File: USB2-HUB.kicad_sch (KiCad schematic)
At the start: 31 parts, among them J11 USB_OTG, J13 690-008-221-904, U13 FSUSB42MUX, U4 TPD4EUSB30, U6 USB2514B-I/M2, U7 AP22653W6, Y1 24MHz

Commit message: added a lot more parts
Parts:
- C11, C14, C15, C3, C4, C7: value 100n -> 0.1uF; DK (none) -> 478-KGM05AR71C104KHCT-ND; PARTNO (none) -> KGM05AR71C104KH; Part Description 0.1uF 10% 16V Ceramic Capacitor X7R 0402 (1005 Metric) -> (none)
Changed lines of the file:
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@@
       (effects (font (size 1.27 1.27)) (justify left))
     )
-    (property "Value" "100n" (at 119.761 170.053 0)
+    (property "Value" "0.1uF" (at 119.761 170.053 0)
       (effects (font (size 1.27 1.27)) (justify left))
     )
@@
       (effects (font (size 1.27 1.27)) hide)
     )
-    (property "Part Description" "	0.1uF 10% 16V Ceramic Capacitor X7R 0402 (1005 Metric)" (at 116.84 168.91 0)
+    (property "Part Description" "" (at 116.84 168.91 0)
       (effects (font (size 1.27 1.27)) hide)
     )
@@
       (effects (font (size 1.27 1.27)) hide)
     )
+    (property "DK" "478-KGM05AR71C104KHCT-ND" (at 116.84 168.91 0)
+      (effects (font (size 1.27 1.27)) hide)
+    )
+    (property "PARTNO" "KGM05AR71C104KH" (at 116.84 168.91 0)
+      (effects (font (size 1.27 1.27)) hide)
+    )
     (pin "1")
     (pin "2")
@@
       (effects (font (size 1.27 1.27)) (justify left))
     )
-    (property "Value" "100n" (at 131.191 170.053 0)
+    (property "Value" "0.1uF" (at 131.191 170.053 0)
       (effects (font (size 1.27 1.27)) (justify left))
     )
@@
       (effects (font (size 1.27 1.27)) hide)
     )
-    (property "Part Description" "	0.1uF 10% 16V Ceramic Capacitor X7R 0402 (1005 Metric)" (at 128.27 168.91 0)
+    (property "Part Description" "" (at 128.27 168.91 0)
       (effects (font (size 1.27 1.27)) hide)
     )
@@
       (effects (font (size 1.27 1.27)) hide)
     )
+    (property "DK" "478-KGM05AR71C104KHCT-ND" (at 128.27 168.91 0)
+      (effects (font (size 1.27 1.27)) hide)
+    )
+    (property "PARTNO" "KGM05AR71C104KH" (at 128.27 168.91 0)
+      (effects (font (size 1.27 1.27)) hide)
+    )
     (pin "1")
     (pin "2")
@@
       (effects (font (size 1.27 1.27)) (justify left))
     )
-    (property "Value" "100n" (at 141.351 170.053 0)
+    (property "Value" "0.1uF" (at 141.351 170.053 0)
       (effects (font (size 1.27 1.27)) (justify left))
     )
@@
       (effects (font (size 1.27 1.27)) hide)
     )
-    (property "Part Description" "	0.1uF 10% 16V Ceramic Capacitor X7R 0402 (1005 Metric)" (at 138.43 168.91 0)
+    (property "Part Description" "" (at 138.43 168.91 0)
       (effects (font (size 1.27 1.27)) hide)
     )
@@
       (effects (font (size 1.27 1.27)) hide)
     )
+    (property "DK" "478-KGM05AR71C104KHCT-ND" (at 138.43 168.91 0)
+      (effects (font (size 1.27 1.27)) hide)
+    )
+    (property "PARTNO" "KGM05AR71C104KH" (at 138.43 168.91 0)
+      (effects (font (size 1.27 1.27)) hide)
+    )
     (pin "1")
     (pin "2")
@@
       (effects (font (size 1.27 1.27)) (justify left))
     )
-    (property "Value" "100n" (at 96.139 170.053 0)
+    (property "Value" "0.1uF" (at 96.139 170.053 0)
       (effects (font (size 1.27 1.27)) (justify left))
     )
@@
       (effects (font (size 1.27 1.27)) hide)
     )
-    (property "Part Description" "	0.1uF 10% 16V Ceramic Capacitor X7R 0402 (1005 Metric)" (at 93.218 168.91 0)
+    (property "Part Description" "" (at 93.218 168.91 0)
       (effects (font (size 1.27 1.27)) hide)
     )
     (property "Field8" "110091611" (at 93.218 168.91 0)
+      (effects (font (size 1.27 1.27)) hide)
+    )
+    (property "DK" "478-KGM05AR71C104KHCT-ND" (at 93.218 168.91 0)
+      (effects (font (size 1.27 1.27)) hide)
+    )
+    (property "PARTNO" "KGM05AR71C104KH" (at 93.218 168.91 0)
       (effects (font (size 1.27 1.27)) hide)
     )
@@
       (effects (font (size 1.27 1.27)) (justify left))
     )
-    (property "Value" "100n" (at 106.299 170.053 0)
+    (property "Value" "0.1uF" (at 106.299 170.053 0)
       (effects (font (size 1.27 1.27)) (justify left))
     )
@@
       (effects (font (size 1.27 1.27)) hide)
     )
-    (property "Part Description" "	0.1uF 10% 16V Ceramic Capacitor X7R 0402 (1005 Metric)" (at 103.378 168.91 0)
+    (property "Part Description" "" (at 103.378 168.91 0)
       (effects (font (size 1.27 1.27)) hide)
     )
@@
       (effects (font (size 1.27 1.27)) hide)
     )
+    (property "DK" "478-KGM05AR71C104KHCT-ND" (at 103.378 168.91 0)
+      (effects (font (size 1.27 1.27)) hide)
+    )
+    (property "PARTNO" "KGM05AR71C104KH" (at 103.378 168.91 0)
+      (effects (font (size 1.27 1.27)) hide)
+    )
     (pin "1")
     (pin "2")
@@
       (effects (font (size 1.27 1.27)) (justify left))
     )
-    (property "Value" "100n" (at 151.765 170.053 0)
+    (property "Value" "0.1uF" (at 151.765 170.053 0)
       (effects (font (size 1.27 1.27)) (justify left))
     )
@@
       (effects (font (size 1.27 1.27)) hide)
     )
-    (property "Part Description" "	0.1uF 10% 16V Ceramic Capacitor X7R 0402 (1005 Metric)" (at 148.844 168.91 0)
+    (property "Part Description" "" (at 148.844 168.91 0)
       (effects (font (size 1.27 1.27)) hide)
     )
@@
       (effects (font (size 1.27 1.27)) hide)
     )
+    (property "DK" "478-KGM05AR71C104KHCT-ND" (at 148.844 168.91 0)
+      (effects (font (size 1.27 1.27)) hide)
+    )
+    (property "PARTNO" "KGM05AR71C104KH" (at 148.844 168.91 0)
+      (effects (font (size 1.27 1.27)) hide)
+    )

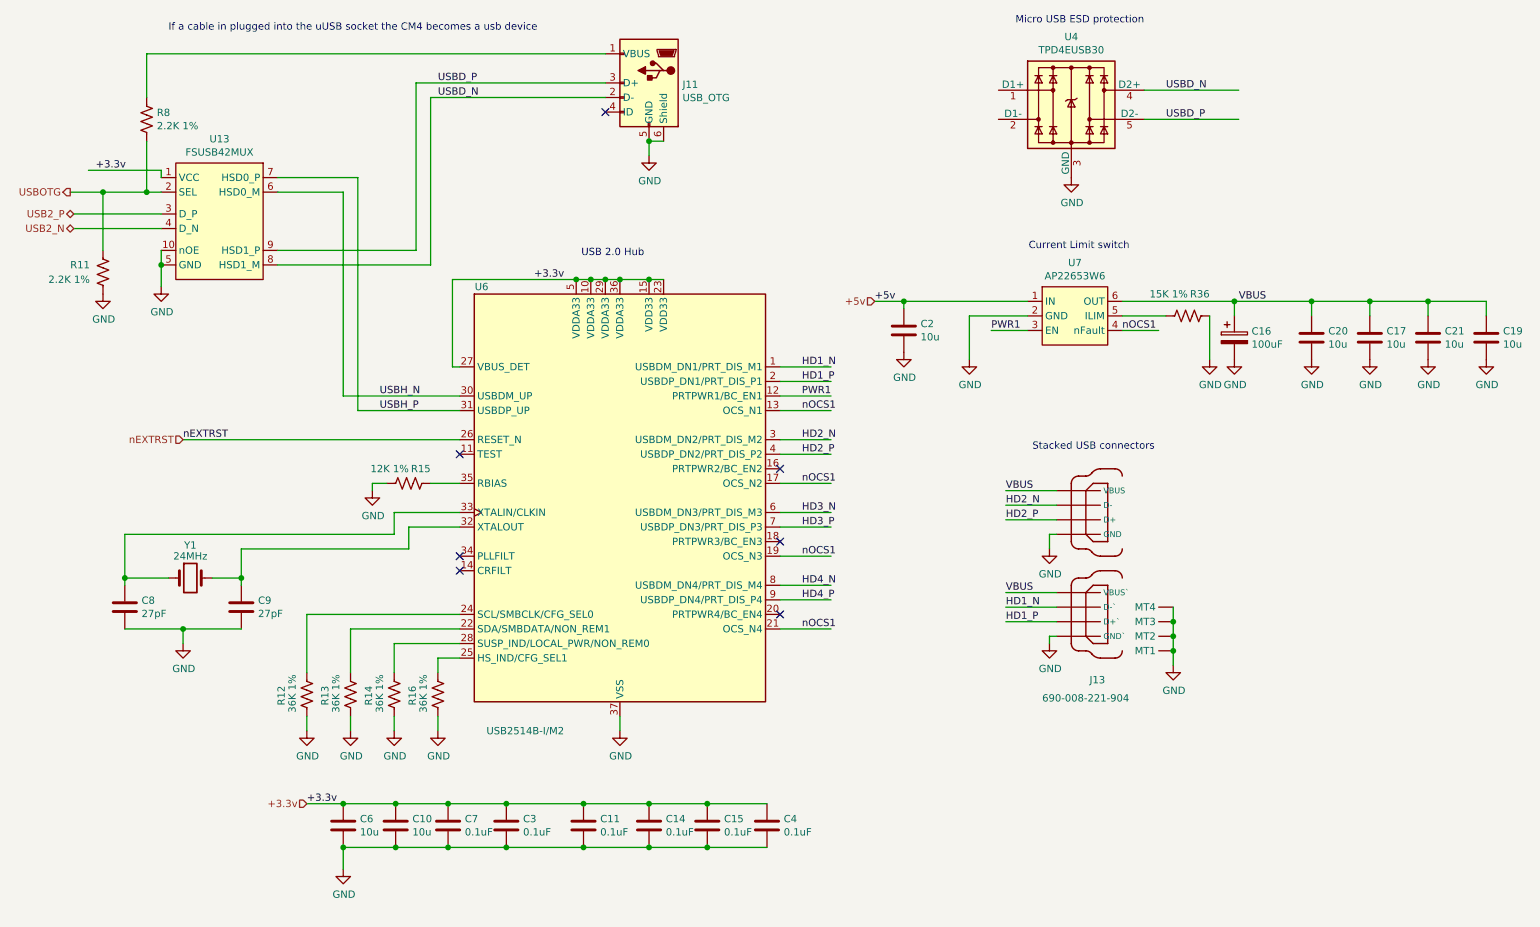
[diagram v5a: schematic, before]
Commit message: resolved some schematic-board errors. switched to tap-on-top ethernet.
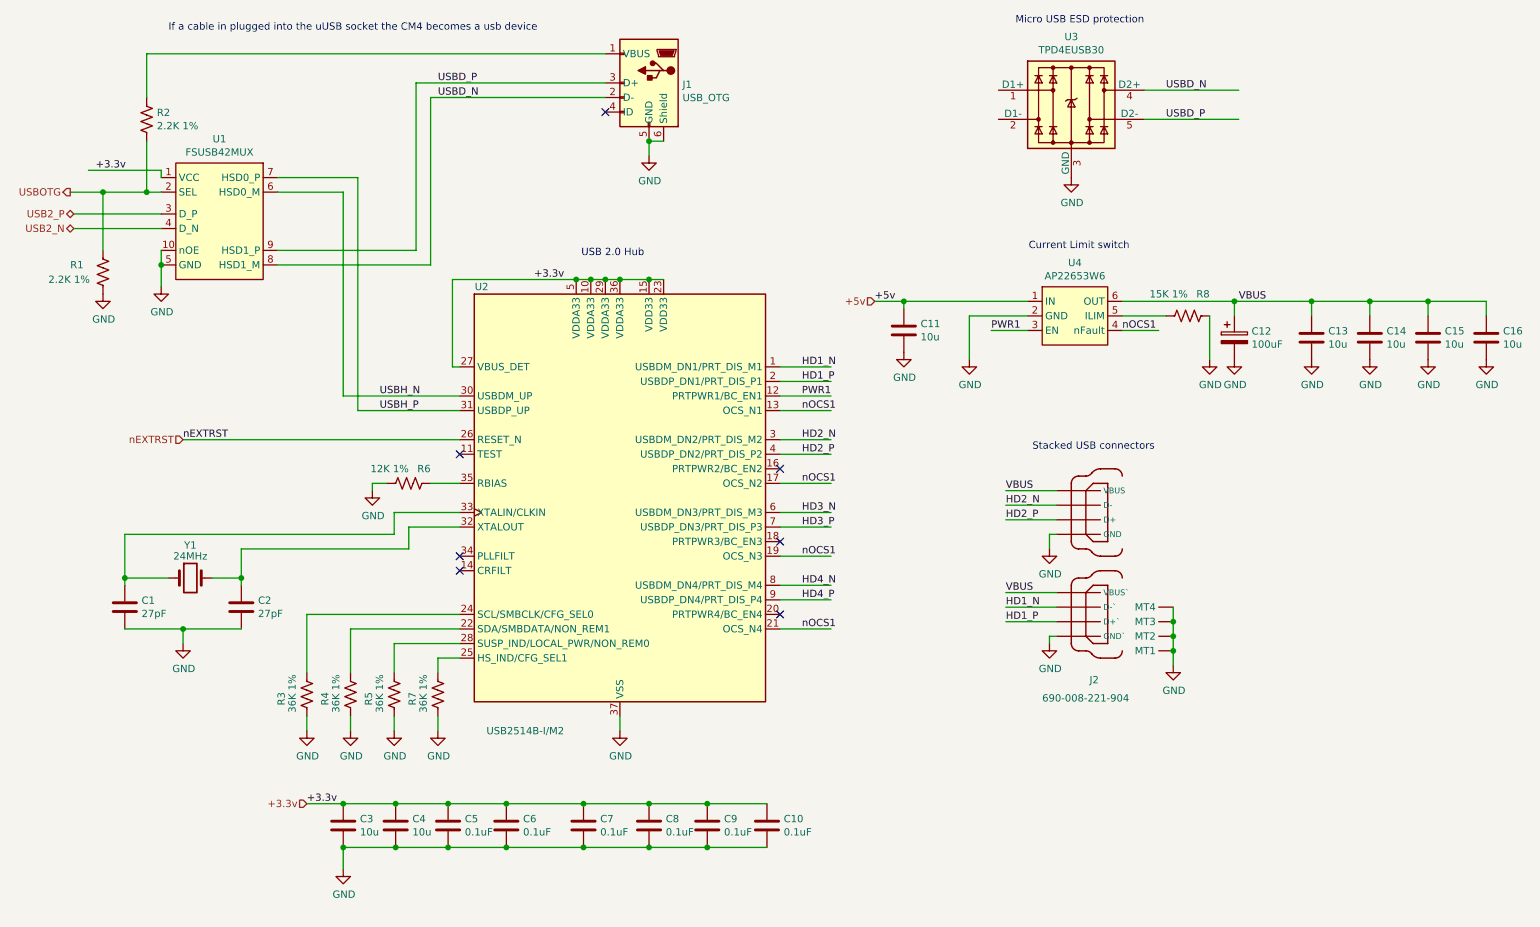
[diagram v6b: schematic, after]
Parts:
- Y1: symbol Device:Crystal_13 -> bitcart:Crystal_13-4pin
- renumbered C8 to C1, C4 to C10, C2 to C11, C16 to C12, C20 to C13, C17 to C14, C21 to C15, C19 to C16, C9 to C2, C6 to C3, C10 to C4, C7 to C5, C3 to C6, C11 to C7, C14 to C8, C15 to C9, J11 to J1, J13 to J2, R11 to R1, R8 to R2, R12 to R3, R13 to R4, R14 to R5, R15 to R6, R16 to R7, R36 to R8, U13 to U1, U6 to U2, U4 to U3, U7 to U4
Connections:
- new net: Y1.2, Y1.4

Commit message: pulled in bitcrane fan and data connectors and edge cuts. most placement done. started routing
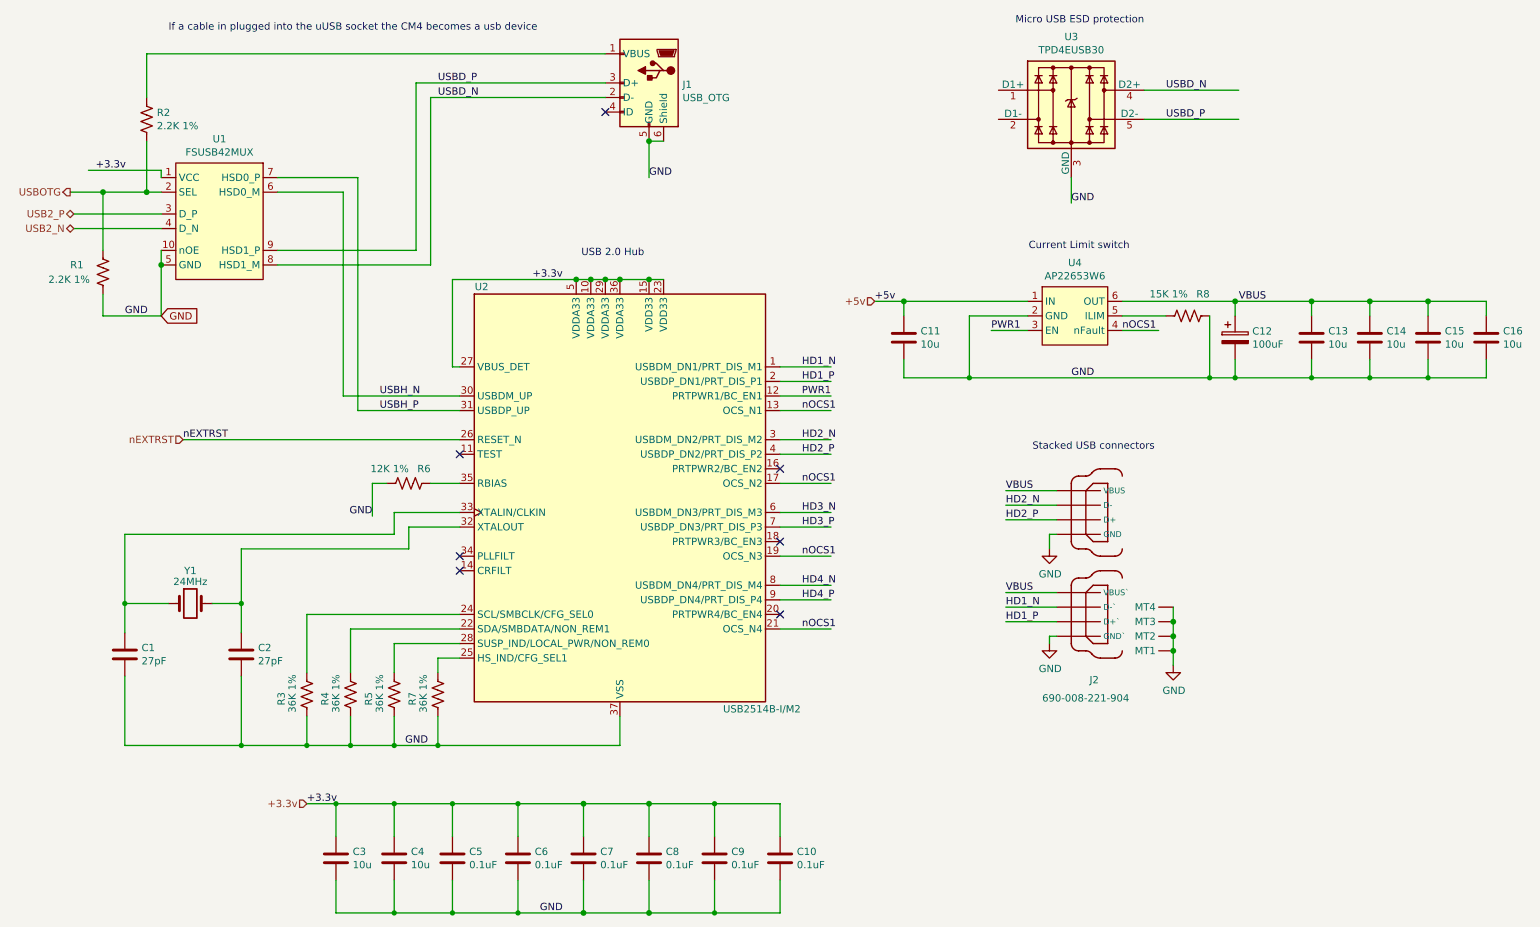
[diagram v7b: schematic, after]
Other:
- moved on the sheet: C1, C10, C11, C2, C3, C4, C5, C6, C7, C8, C9, Y1

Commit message: more placement
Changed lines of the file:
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@@
-    (stroke (width 0) (type solid))
-  )
-  (wire (pts (xy 43.18 55.88) (xy 43.18 54.61))
     (stroke (width 0) (type solid))
   )
@@
     (stroke (width 0) (type solid))
   )
-  (wire (pts (xy 30.48 54.61) (xy 43.18 54.61))
+  (wire (pts (xy 30.48 55.88) (xy 43.18 55.88))
     (stroke (width 0) (type solid))
   )
@@
     (effects (font (size 1.27 1.27)) (justify left bottom))
   )
-  (label "+3.3v" (at 31.75 54.61 0) (fields_autoplaced)
+  (label "+3.3v" (at 31.75 55.88 0) (fields_autoplaced)
     (effects (font (size 1.27 1.27)) (justify left bottom))
   )
